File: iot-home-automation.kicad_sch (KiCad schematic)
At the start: 25 parts, among them J1 Conn_01x05_Pin, J2 Conn_01x08_Pin, J3 Conn_01x02_Pin, J4 Conn_02x08_Odd_Even, J6 Conn_01x02_Pin, Q1 PMOS, SW1 SW_Push_SPDT, U1 STM32WB5MMGH6TR, U2 SHTC3, U3 AP2127K-1.8, U4 OPT3001DNPT

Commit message: sent for prod
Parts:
- removed C3: 1uF, Capacitor_SMD:C_0603_1608Metric, symbol Device:C
- removed J6: Conn_01x02_Pin, Connector_PinHeader_2.54mm:PinHeader_1x02_P2.54mm_Vertical, symbol Connector:Conn_01x02_Pin
- removed R1: 220K, Resistor_SMD:R_0603_1608Metric, symbol Device:R
- removed U3: AP2127K-1.8, Package_TO_SOT_SMD:SOT-23-5, symbol Regulator_Linear:AP2127K-1.8
- added C1, C2: 10u, Capacitor_SMD:C_0603_1608Metric, symbol Device:C
- added C6: 100nF, Capacitor_SMD:C_0603_1608Metric, symbol Device:C
- added L1: 10u, Inductor_SMD:L_Changjiang_FNR6028S, symbol Device:L
- added U2: TPS62202DBV, Package_TO_SOT_SMD:SOT-23-5, symbol Regulator_Switching:TPS62202DBV
- C4: value 1uF -> 100nF; Link https://www.digikey.ca/en/products/detail/samsung-electro-mechanics/CL10B105KP8NNNC/3887604 -> https://www.digikey.ca/en/products/detail/samsung-electro-mechanics/CL03A104KQ3NNNC/3886671
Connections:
- net +BATT: now also J2.6 (Pin_6)
- net Door_EXTI: now also C6.1
- net GND: now also C1.2, C2.2, C6.2, U2.2 (GND)
- net MCU_RX1: now also J2.3 (Pin_3); no longer J2.4 (Pin_4)
- net MCU_TX1: now also J2.2 (Pin_2); no longer J2.3 (Pin_3)
- net PB3: now also J2.4 (Pin_4); no longer J2.5 (Pin_5)
- net PD1: now also J2.5 (Pin_5); no longer J2.6 (Pin_6)
- net Vtherm: now also C4.1
- net LIGHT_IRQ: now reaches R1.2, U4.5 (INT)
- net LIGHT_IRQ: now also U1.19 (PB5)
- net VDD_THERM: now reaches U1.14 (PB8)
- net VDD_THERM: now also R1.1
- net +1V8 renamed VDD
- net VDD: now also SW1.3 (C), U1.15 (VBAT), U1.17 (VDD), U1.4 (VREF+), U1.6 (VDDA), C2.1, L1.2, U2.4 (FB); no longer R1.1
- removed net +3V0: C4.1, D1.2 (A2), J2.2 (Pin_2), J3.2 (Pin_2), Q1.3 (S), R1.1, SW1.3 (C), U1.15 (VBAT), U1.17 (VDD), U1.4 (VREF+), U1.6 (VDDA)
- net LDO_EN: no longer names the net of U1.36 (PC6)
- new net: L1.1, U2.5 (SW)
- new net VCC: C1.1, D1.2 (A2), J3.2 (Pin_2), Q1.3 (S), R1.1, U2.1 (VI), U2.3 (EN)
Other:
- note added: "Battery life calculator (link)"
- note added: "MCU"
- note added: "VDD = 1V8 so SMPS Bypass Mode See AN5246"
- note removed: "3V0 = MCU SMPS IN + Door + Buzzer 1V8 = rest of board power"
- note removed: "Bypass LDO En for dev"
- note removed: "Limit switch with 1 NO and 1 NC port. Must Pullup to 3V0 since 1V8 is only ON when MCU is active"
- note removed: "MCU, uses embedded SMPS"
- moved on the sheet: C2, J1, J2, J4, LS1, Q1, R1, SW1, TH1, U2, U4

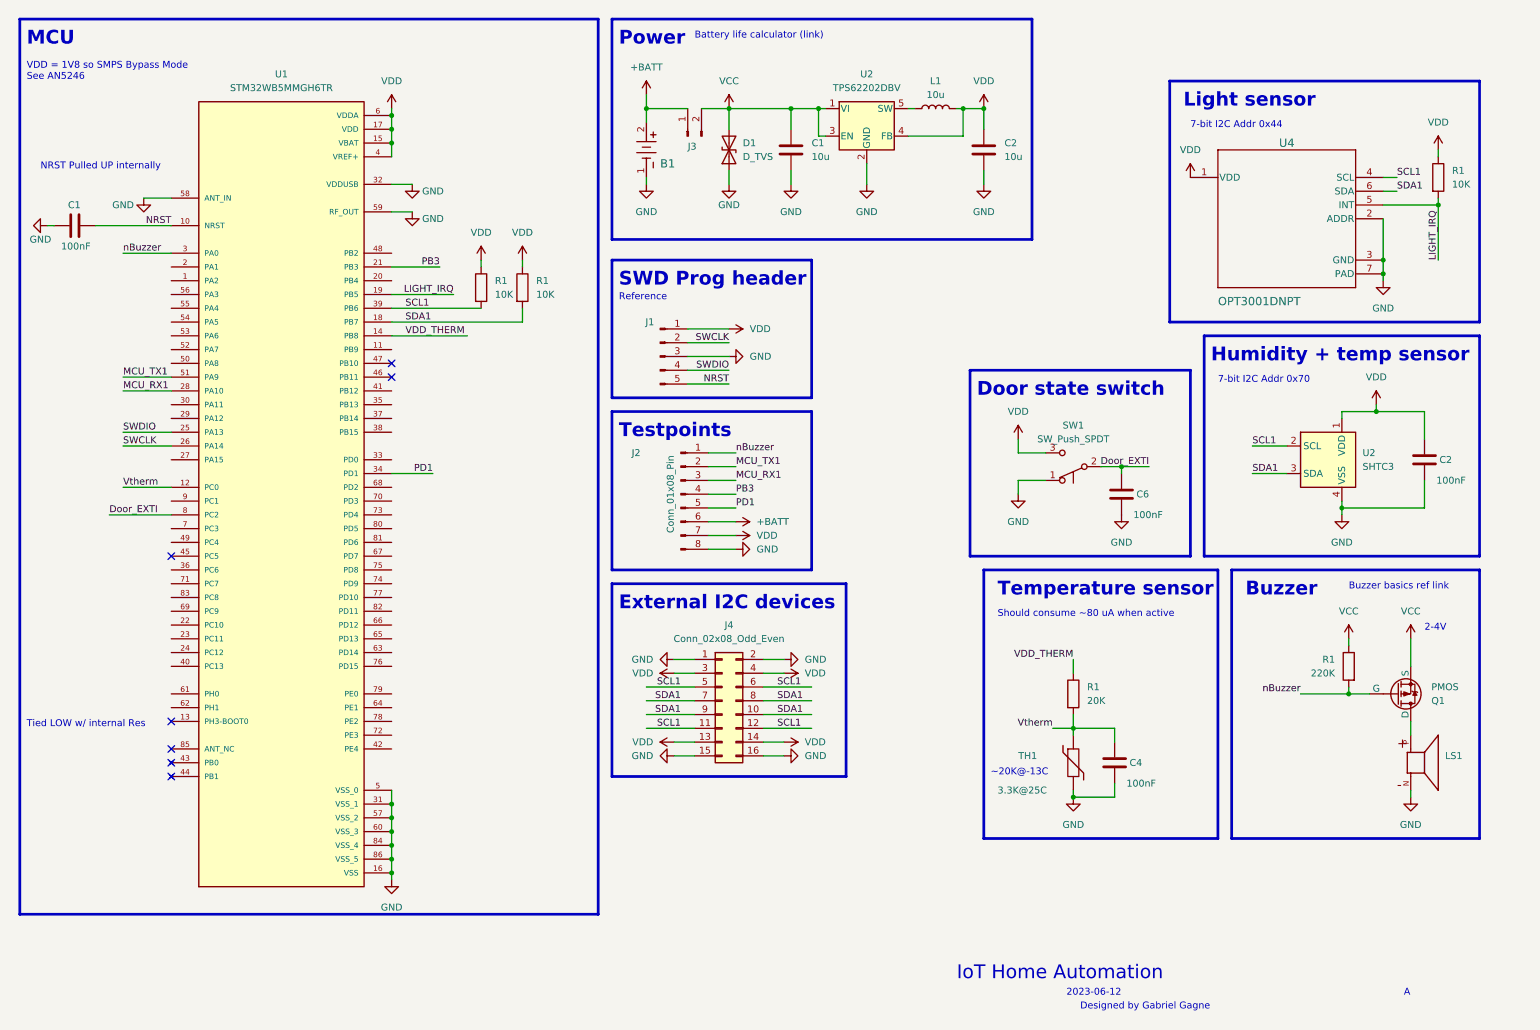
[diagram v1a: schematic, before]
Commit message: Schematic and first routing pass done
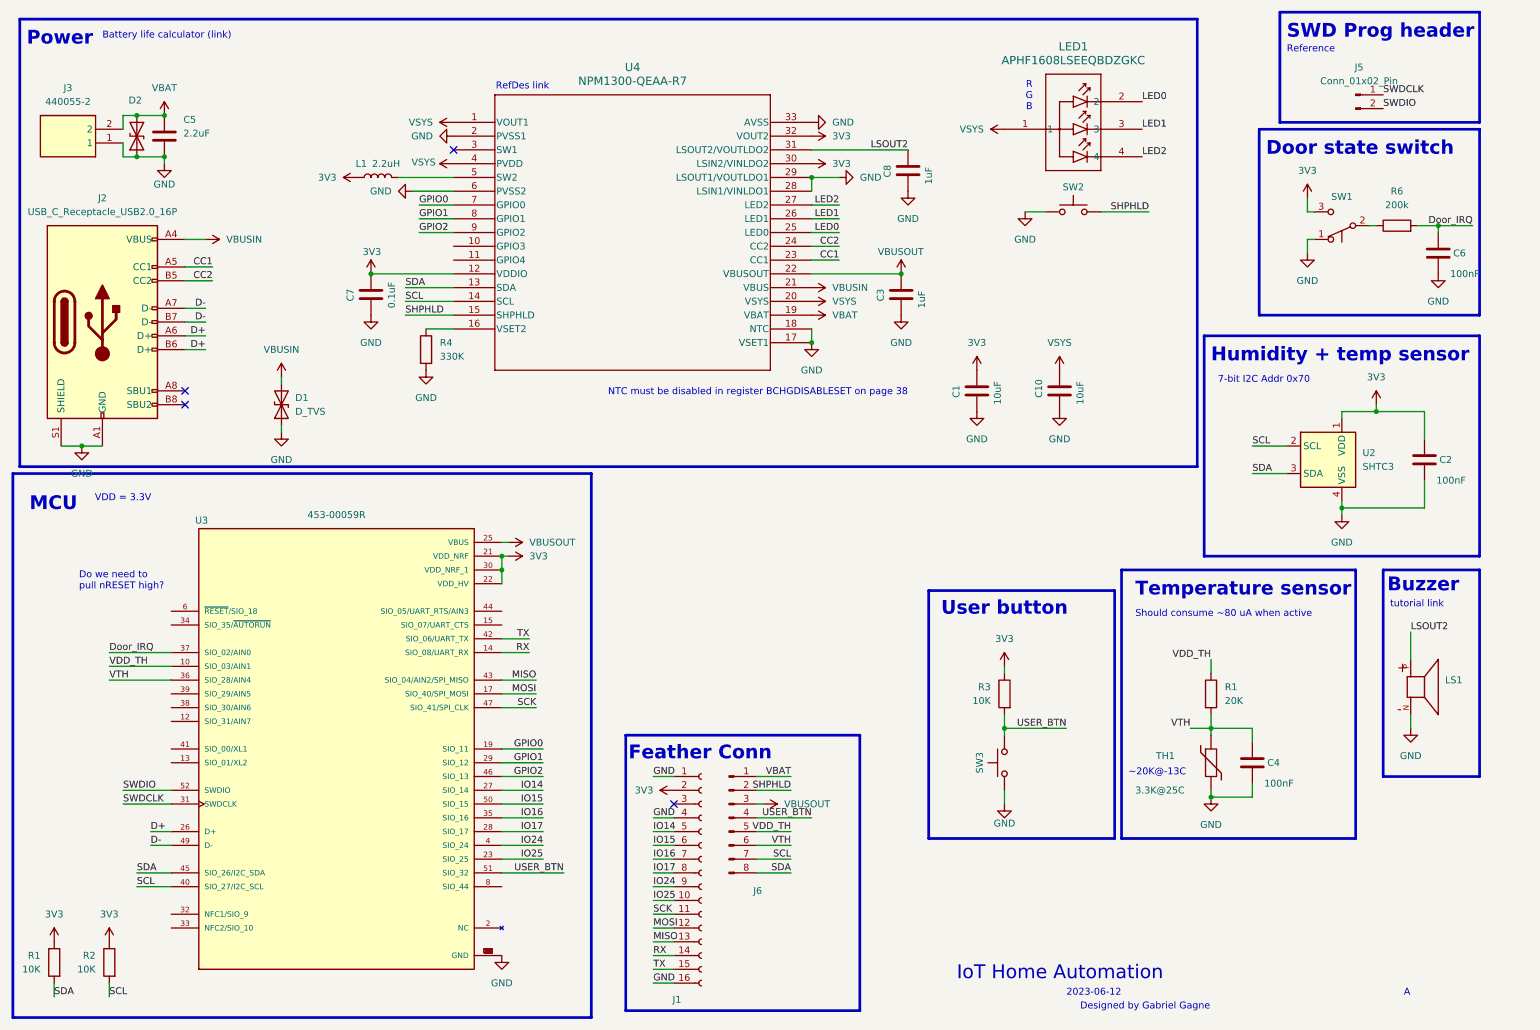
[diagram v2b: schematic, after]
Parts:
- removed B1: BU2032SM-JJ-GTR, BU2032SM-JJ-GTR:BU2032SM-JJ-GTR_MPD, symbol BU2032SM-JJ-GTR:BU2032SM-JJ-GTR
- removed C1: 100nF, Capacitor_SMD:C_0603_1608Metric, symbol Device:C
- removed C1, C2: 10u, Capacitor_SMD:C_0603_1608Metric, symbol Device:C
- removed J1: Conn_01x05_Pin, Connector_PinHeader_2.54mm:PinHeader_1x05_P2.54mm_Vertical, symbol Connector:Conn_01x05_Pin
- removed J2: Conn_01x08_Pin, Connector_PinHeader_2.54mm:PinHeader_1x08_P2.54mm_Vertical, symbol Connector:Conn_01x08_Pin
- removed J3: Conn_01x02_Pin, Connector_PinHeader_2.54mm:PinHeader_1x02_P2.54mm_Vertical, symbol Connector:Conn_01x02_Pin
- removed J4: Conn_02x08_Odd_Even, Connector_PinHeader_2.54mm:PinHeader_2x08_P2.54mm_Vertical, symbol Connector_Generic:Conn_02x08_Odd_Even
- removed Q1: PMOS, Package_TO_SOT_SMD:SOT-723, symbol Simulation_SPICE:PMOS
- removed R1: 220K, Resistor_SMD:R_0603_1608Metric, symbol Device:R
- removed R1 (x3): 10K, Resistor_SMD:R_0603_1608Metric, symbol Device:R
- removed U1: STM32WB5MMGH6TR, STM32WB5MMGH6TR:XCVR_STM32WB5MMGH6TR, symbol STM32WB5MMGH6TR:STM32WB5MMGH6TR
- removed U2: TPS62202DBV, Package_TO_SOT_SMD:SOT-23-5, symbol Regulator_Switching:TPS62202DBV
- removed U4: OPT3001DNPT, Package_SON:WSON-6-1EP_2x2mm_P0.65mm_EP1x1.6mm, symbol OPT3001:OPT3001DNPT
- added C1, C10: 10uF, Capacitor_SMD:C_0603_1608Metric, symbol Device:C
- added C3, C8: 1uF, Capacitor_SMD:C_0603_1608Metric, symbol Device:C
- added C5: 2.2uF, Capacitor_SMD:C_0603_1608Metric, symbol Device:C
- added C7: 0.1uF, Capacitor_SMD:C_0603_1608Metric, symbol Device:C
- added D2: D_TVS, Diode_SMD:D_SOD-323F, symbol Device:D_TVS
- added J1: Conn_01x16_Female, Connector_PinHeader_2.54mm:PinHeader_1x16_P2.54mm_Vertical, symbol Connector:Conn_01x16_Female
- added J2: USB_C_Receptacle_USB2.0_16P, Connector_USB:USB_C_Receptacle_JAE_DX07S016JA1R1500, symbol Connector:USB_C_Receptacle_USB2.0_16P
- added J3: 440055-2, jst:SHDRRA2W50P0X200_1X2_600X770X525P, symbol 440055-2:440055-2
- added J5: Conn_01x02_Pin, Connector_PinHeader_2.54mm:PinHeader_1x02_P2.54mm_Vertical, symbol Connector:Conn_01x02_Pin
- added J6: Conn_01x08_Pin, Connector_PinHeader_2.54mm:PinHeader_1x08_P2.54mm_Vertical, symbol Connector:Conn_01x08_Pin
- added LED1: APHF1608LSEEQBDZGKC, ul_APHF1608LSEEQBDZGKC:APHF_KNB, symbol 2025-01-14_20-58-26:APHF1608LSEEQBDZGKC
- added R1, R2, R3: 10K, Resistor_SMD:R_0603_1608Metric, symbol Device:R
- added R4: 330K, Resistor_SMD:R_0603_1608Metric, symbol Device:R
- added R6: 200k, Resistor_SMD:R_0603_1608Metric, symbol Device:R
- added SW2, SW3: SW_Push, Button_Switch_SMD:SW_SPST_PTS810, symbol Switch:SW_Push
- added U3: 453-00059R, 453-00059R:XCVR_453-00059R, symbol 453-00059R:453-00059R
- added U4: NPM1300-QEAA-R7, ul_NPM1300-QEAA-R7:QFN32_5X5_NOR, symbol 2025-01-14_19-50-05:NPM1300-QEAA-R7
- L1: value 10u -> 2.2uH; footprint Inductor_SMD:L_Changjiang_FNR6028S -> Inductor_SMD:L_Murata_DFE201610P; Link https://www.digikey.ca/en/products/detail/taiyo-yuden/NRS60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 -> (none)
- SW1: footprint Connector_PinHeader_2.54mm:PinHeader_1x03_P2.54mm_Vertical -> CL-DA-1BB4-A2T:CLDA1BB4A2T; Link Any microswitch -> https://www.digikey.ca/en/products/detail/nidec-components-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
- TH1: footprint Resistor_THT:R_Axial_DIN0204_L3.6mm_D1.6mm_P7.62mm_Horizontal -> (none)
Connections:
- net GND: now also C1.2, C10.2, C3.2, C5.2, C7.2, C8.2, D2.1 (A1), J1.1 (Pin_1), J1.16 (Pin_16), J1.4 (Pin_4), J2.A1 (GND), J2.A12 (GND), J2.B1 (GND), J2.B12 (GND), J2.S1 (SHIELD), J3.1, R4.2, SW2.1, SW3.1, U3.1 (GND), U3.11 (GND), U3.16 (GND), U3.18 (GND), U3.20 (GND), U3.24 (GND), U3.3 (GND), U3.48 (GND), U3.5 (GND), U3.7 (GND), U3.9 (GND), U3.G1 (GND), U3.G2 (GND), U3.G3 (GND), U3.G4 (GND), U3.G5 (GND), U3.G6 (GND), U3.G7 (GND), U4.17 (VSET1), U4.18 (NTC), U4.2 (PVSS1), U4.28 (LSIN1/VINLDO1), U4.29 (LSOUT1/VOUTLDO1), U4.33 (AVSS), U4.6 (PVSS2)
- net SWDIO: now also J5.2 (Pin_2), U3.52 (SWDIO)
- net 3V3: now reaches L1.1
- net 3V3: now also C2.1, SW1.3 (C), U2.1 (VDD), C1.1, C7.1, J1.2 (Pin_2), R1.1, R2.1, R3.1, U3.21 (VDD_NRF), U3.22 (VDD_HV), U3.30 (VDD_NRF_1), U4.12 (VDDIO), U4.30 (LSIN2/VINLDO2), U4.32 (VOUT2)
- net LSOUT2: now reaches LS1.P
- net LSOUT2: now also C8.1, U4.31 (LSOUT2/VOUTLDO2)
- net Door_EXTI: no longer names the net of SW1.2 (B)
- net Door_EXTI: now also R6.1; no longer C6.1
- net SCL1 renamed SCL
- net SCL: now also J6.7 (Pin_7), R2.2, U3.40 (SIO_27/I2C_SCL), U4.14 (SCL)
- net SDA1 renamed SDA
- net SDA: now also J6.8 (Pin_8), R1.2, U3.45 (SIO_26/I2C_SDA), U4.13 (SDA)
- net VCC renamed VBUSIN
- net VBUSIN: now also J2.A4 (VBUS), J2.A9 (VBUS), J2.B4 (VBUS), J2.B9 (VBUS), U4.21 (VBUS)
- removed net VDD: C2.1, L1.2, SW1.3 (C), U2.1 (VDD)
- net VDD_THERM renamed VDD_TH
- net VDD_TH: now also J6.5 (Pin_5), U3.10 (SIO_03/AIN1)
- net Vtherm renamed VTH
- net VTH: now also J6.6 (Pin_6), U3.36 (SIO_28/AIN4)
- new net: L1.2, U4.5 (SW2)
- new net: R4.1, U4.16 (VSET2)
- new net CC1: J2.A5 (CC1), U4.23 (CC1)
- new net CC2: J2.B5 (CC2), U4.24 (CC2)
- new net D+: J2.A6 (D+), J2.B6 (D+), U3.26 (D+)
- new net D-: J2.A7 (D-), J2.B7 (D-), U3.49 (D-)
- new net Door_IRQ: C6.1, R6.2, U3.37 (SIO_02/AIN0)
- new net GPIO0: U3.19 (SIO_11), U4.7 (GPIO0)
- new net GPIO1: U3.29 (SIO_12), U4.8 (GPIO1)
- new net GPIO2: U3.46 (SIO_13), U4.9 (GPIO2)
- new net IO14: J1.5 (Pin_5), U3.27 (SIO_14)
- new net IO15: J1.6 (Pin_6), U3.50 (SIO_15)
- new net IO16: J1.7 (Pin_7), U3.35 (SIO_16)
- new net IO17: J1.8 (Pin_8), U3.28 (SIO_17)
- new net IO24: J1.9 (Pin_9), U3.4 (SIO_24)
- new net IO25: J1.10 (Pin_10), U3.23 (SIO_25)
- new net LED0: LED1.2, U4.25 (LED0)
- new net LED1: LED1.3, U4.26 (LED1)
- new net LED2: LED1.4, U4.27 (LED2)
- new net MISO: J1.13 (Pin_13), U3.43 (SIO_04/AIN2/SPI_MISO)
- new net MOSI: J1.12 (Pin_12), U3.17 (SIO_40/SPI_MOSI)
- new net RX: J1.14 (Pin_14), U3.14 (SIO_08/UART_RX)
- new net SCK: J1.11 (Pin_11), U3.47 (SIO_41/SPI_CLK)
- new net SHPHLD: J6.2 (Pin_2), SW2.2, U4.15 (SHPHLD)
- new net SWDCLK: J5.1 (Pin_1), U3.31 (SWDCLK)
- new net TX: J1.15 (Pin_15), U3.42 (SIO_06/UART_TX)
- new net USER_BTN: J6.4 (Pin_4), R3.2, SW3.2, U3.51 (SIO_32)
- new net VBAT: C5.1, D2.2 (A2), J3.2, J6.1 (Pin_1), U4.19 (VBAT)
- new net VBUSOUT: C3.1, J6.3 (Pin_3), U3.25 (VBUS), U4.22 (VBUSOUT)
- new net VSYS: C10.1, LED1.1, U4.1 (VOUT1), U4.20 (VSYS), U4.4 (PVDD)
- no-connect marks 7 -> 4
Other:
- note added: "Do we need to pull nRESET high?"
- note added: "Feather Conn"
- note added: "NTC must be disabled in register BCHGDISABLESET on page 38"
- note added: "R G B"
- note added: "RefDes link"
- note added: "User button"
- note added: "VDD = 3.3V"
- note added: "tutorial link"
- note removed: "2-4V"
- note removed: "7-bit I2C Addr 0x44"
- note removed: "Buzzer basics ref link"
- note removed: "External I2C devices"
- note removed: "Light sensor"
- note removed: "NRST Pulled UP internally"
- note removed: "Testpoints"
- note removed: "Tied LOW w/ internal Res"
- note removed: "VDD = 1V8 so SMPS Bypass Mode See AN5246"
- moved on the sheet: C4, C6, R1, SW1, TH1

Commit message: Rev A
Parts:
- removed C10: 10uF, Capacitor_SMD:C_0603_1608Metric, symbol Device:C
- removed C7: 0.1uF, Capacitor_SMD:C_0603_1608Metric, symbol Device:C
- added C11, C9: 10uF, Capacitor_SMD:C_0603_1608Metric, symbol Device:C
- C1: value 10uF -> 1uF
- C2, C4, C6: value 100nF -> 0.1uF
- C8: value 1uF -> 10uF
- renumbered R1 to R5
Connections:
- net 3V3: no longer C1.1, L1.1, U4.12 (VDDIO), U4.30 (LSIN2/VINLDO2), U4.32 (VOUT2)
- net GND: now also C11.2, C9.2
- net LSOUT2: now also C1.1; no longer C8.1
- net VSYS: now also C8.1, C9.1
- net at U4.5 (SW2): now also L1.1; no longer L1.2
- new net +3V3: C11.1, L1.2, U4.12 (VDDIO), U4.30 (LSIN2/VINLDO2), U4.32 (VOUT2)
- no-connect marks 4 -> 6
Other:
- note added: "Single via to GND layer"
- moved on the sheet: D1, J1, J6, LED1, R1, R2, SW2, U3

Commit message: RevB done?
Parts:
- removed C6: 0.1uF, Capacitor_SMD:C_0603_1608Metric, symbol Device:C
- removed R6: 200k, Resistor_SMD:R_0603_1608Metric, symbol Device:R
- removed SW1: SW_Push_SPDT, CL-DA-1BB4-A2T:CLDA1BB4A2T, symbol Switch:SW_Push_SPDT
- added S1: CL-DA-1BB4-A2T, CLDA1BB4A2T, symbol CL-DA-1BB4-A2T:CL-DA-1BB4-A2T
- added TP1, TP2: TestPoint, TestPoint:TestPoint_Pad_D1.5mm, symbol Connector:TestPoint
- C5: value 2.2uF -> 10uF
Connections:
- net 3V3 is gone; now on net +3V3: C2.1, J1.2 (Pin_2), R1.1, R2.1, R3.1, U2.1 (VDD), U3.21 (VDD_NRF), U3.22 (VDD_HV), U3.30 (VDD_NRF_1)
- net +3V3: now also J1.3 (Pin_3), J6.4 (Pin_4)
- net D+: now also TP2.1
- net D-: now also TP1.1
- net GND: now also J6.3 (Pin_3), S1.3
- net LSOUT2: now also J1.9 (Pin_9)
- net SHPHLD: no longer J6.2 (Pin_2)
- net USER_BTN: no longer J6.4 (Pin_4)
- net VBUSOUT: now also J6.2 (Pin_2); no longer J6.3 (Pin_3)
- net DOOR_SW: now reaches U3.12 (SIO_31/AIN7)
- net DOOR_SW: now also S1.1
- net Door_IRQ: no longer names the net of U3.37 (SIO_02/AIN0)
- net IO24: no longer names the net of U3.4 (SIO_24)
- net IO24: no longer J1.9 (Pin_9)
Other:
- note added: "1 GPIO as IRQ to MCU"
- note added: "2024-03"
- note added: "Avoid IO24, 44"
- note added: "B"
- note added: "R B G"
- note added: "SWD"
- note added: "To exit hibernate: - VBUS voltage - Pull SHPHLD to GND"
- note added: "When door is closed, S1 is open Configure pullup on DOOR_BTN"
- note added: "nRF52833"
- note removed: "2023-06-12"
- note removed: "A"
- note removed: "R G B"
- note removed: "Reference"
- note removed: "SWD Prog header"
- note removed: "VDD = 3.3V"
- moved on the sheet: J1, J5, J6
